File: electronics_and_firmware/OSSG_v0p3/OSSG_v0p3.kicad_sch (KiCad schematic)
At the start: 77 parts, among them IC1 DW01A, J1 USB_B_Micro, J2 External PDM Mic Input, Q1 FS8205A, Q2 Q_NPN_BEC, Q3 Q_NPN_BEC, SW1 SW_SPST, U1 ESP32-PICO-D4, U2 TP4056, U3 XC6222B331MRG, U4 FT232RQ, U5 APX803L-29SA-7, U6 MP23DB01HPTR

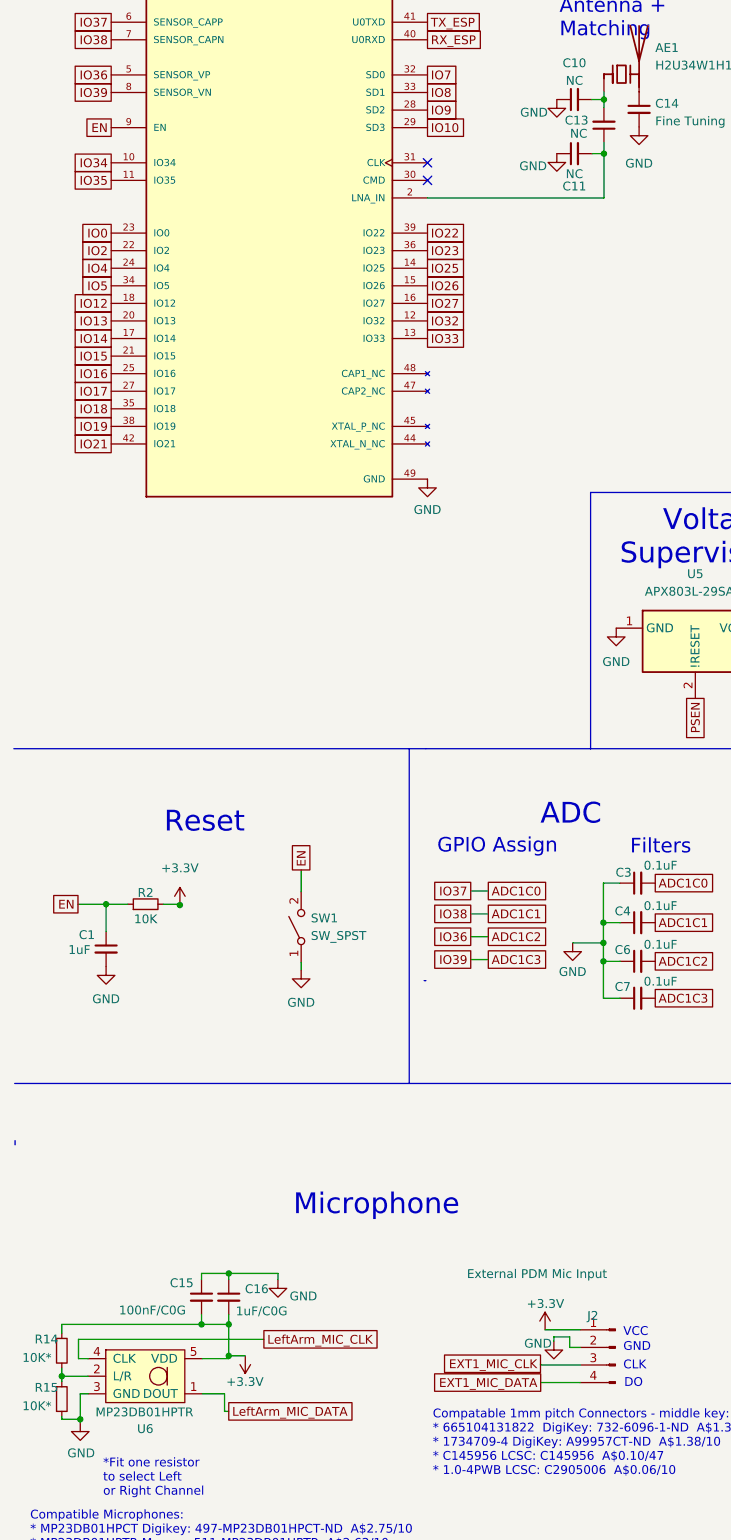
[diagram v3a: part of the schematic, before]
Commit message: start adding in MPN, links, pricing, BOM... digikey and LCSC
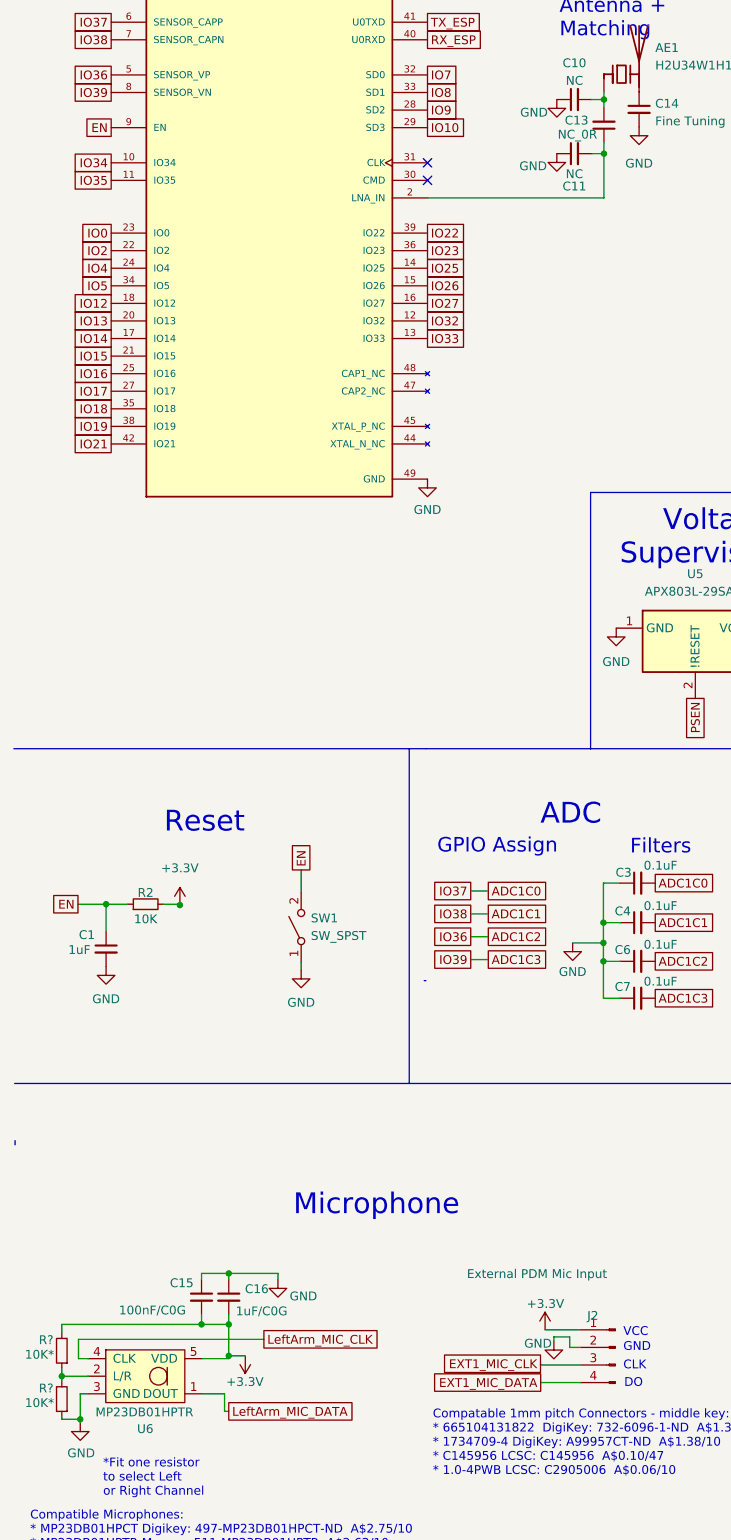
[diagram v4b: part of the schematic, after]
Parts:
- removed R14, R15: 10K*, Resistor_SMD:R_0402_1005Metric, symbol Device:R_Small
- added R? (x2): 10K*, Resistor_SMD:R_0402_1005Metric, symbol Device:R_Small
- AE1: DigiKeyLink (none) -> https://www.digikey.ca/en/products/detail/unictron-technolo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; MPN (none) -> 2047-H2U34W1H1Z0400CT-ND; Price (none) -> 0.9
- C1: DigiKeyLink (none) -> https://www.digikey.ca/en/products/detail/murata-electronic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; MPN (none) -> 490-GRT155C80J105KE01JCT-ND; Price (none) -> 0.0448
- C13: value NC -> NC_0R
- C2: DigiKeyLink (none) -> https://www.digikey.ca/en/products/detail/samsung-electro-m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; MPN (none) -> 1276-1450-1-ND; Price (none) -> 0.1092
- C5: DigiKeyLink (none) -> https://www.digikey.ca/en/products/detail/samsung-electro-m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; MPN (none) -> 1276-1043-1-ND; Price (none) -> 0.006
- IC1: LCSC C351410 -> (none); LCSCLink (none) -> https://lcsc.com/product-detail/Battery-Management-ICs_PUOL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; MPN_LCSC (none) -> C351410; Price (none) -> 0.061
- J1: DigiKeyLink (none) -> https://www.digikey.ca/en/products/detail/molex/1050170001/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; MPN (none) -> WM1399CT-ND; Price (none) -> 1.33
- Q1: LCSCLink (none) -> https://lcsc.com/product-detail/MOSFETs_Fortune-Semicon-FS8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; MPN_LCSC (none) -> C16052; Price (none) -> 0.2665
- R2: DigiKeyLink (none) -> https://www.digikey.ca/en/products/detail/stackpole-electro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; MPN (none) -> RMCF0402JT10K0CT-ND; Price (none) -> 0.018
- R3: DigiKeyLink (none) -> https://www.digikey.ca/en/products/detail/yageo/RC0402JR-07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; MPN (none) -> YAG1279CT-ND; Price (none) -> 0.0182
- SW1: DigiKeyLink (none) -> https://www.digikey.ca/en/products/detail/omron-electronics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; MPN (none) -> SW1103CT-ND; Price (none) -> 1.49
- U1: DigiKeyLink (none) -> https://www.digikey.ca/en/products/detail/espressif-systems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; LCSCLink (none) -> https://lcsc.com/product-detail/RF-Transceiver-ICs_Espressi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; MPN (none) -> 1904-1029-1-ND; MPN_LCSC (none) -> C193707; Price (none) -> 4.1837
- U2: LCSCLink (none) -> https://lcsc.com/product-detail/Battery-Management-ICs_TOPP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; MPN_LCSC (none) -> C21417; Price (none) -> 0.3102
- U3: Price (none) -> 1.25
- U4: LCSCLink (none) -> https://lcsc.com/product-detail/USB-ICs_FTDI-FT232RQ-REEL_C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; MPN_LCSC (none) -> C14090; Price (none) -> 16.1196
- U5: DigiKeyLink (none) -> https://www.digikey.ca/en/products/detail/diodes-incorporat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; MPN (none) -> APX803L-29SA-7DICT-ND; Price (none) -> 0.59
- U6: DigiKeyLink (none) -> https://www.digikey.ca/en/products/detail/stmicroelectronic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; MPN (none) -> 497-MP23DB01HPCT-ND; Price (none) -> 3.31
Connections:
- net +3V3: now also R?.2
- net GND: now also R?.1
- net at U6.2 (L/R): now also R?.1, R?.2

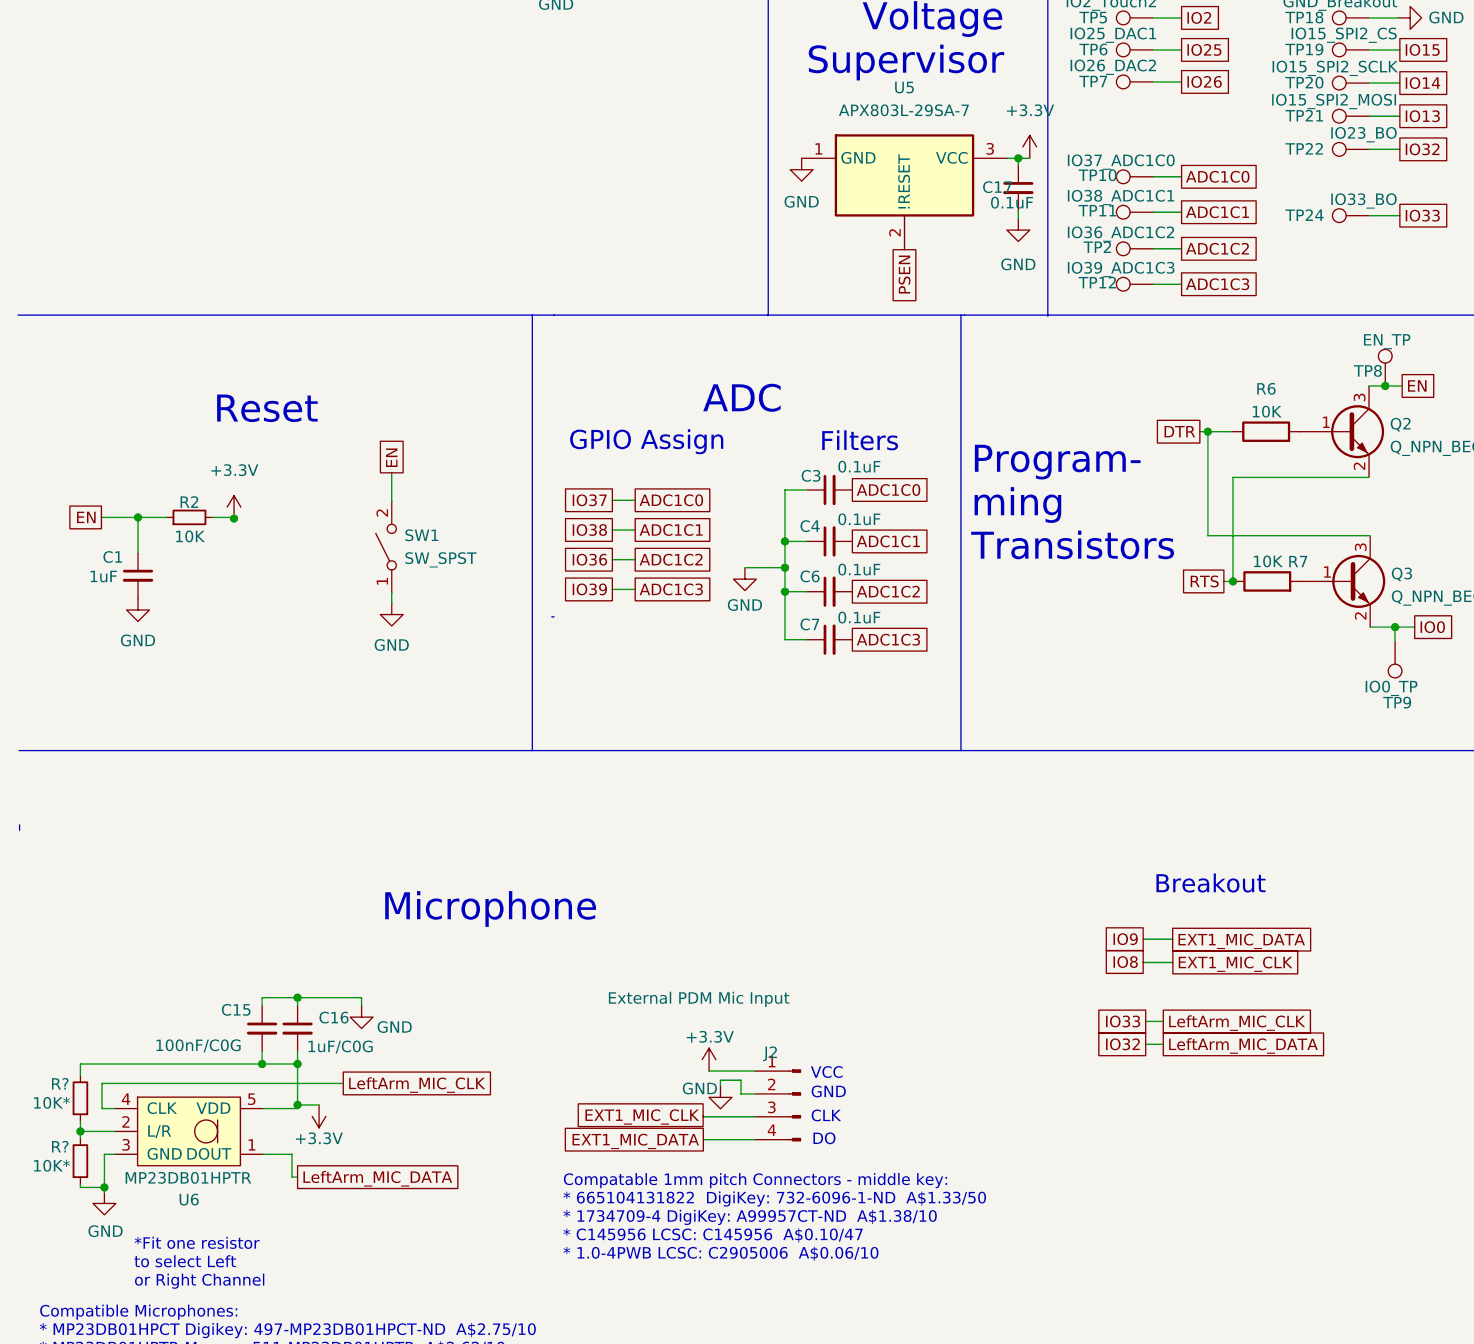
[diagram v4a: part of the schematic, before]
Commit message: add in part numbers and prices for almost all components for LCSC
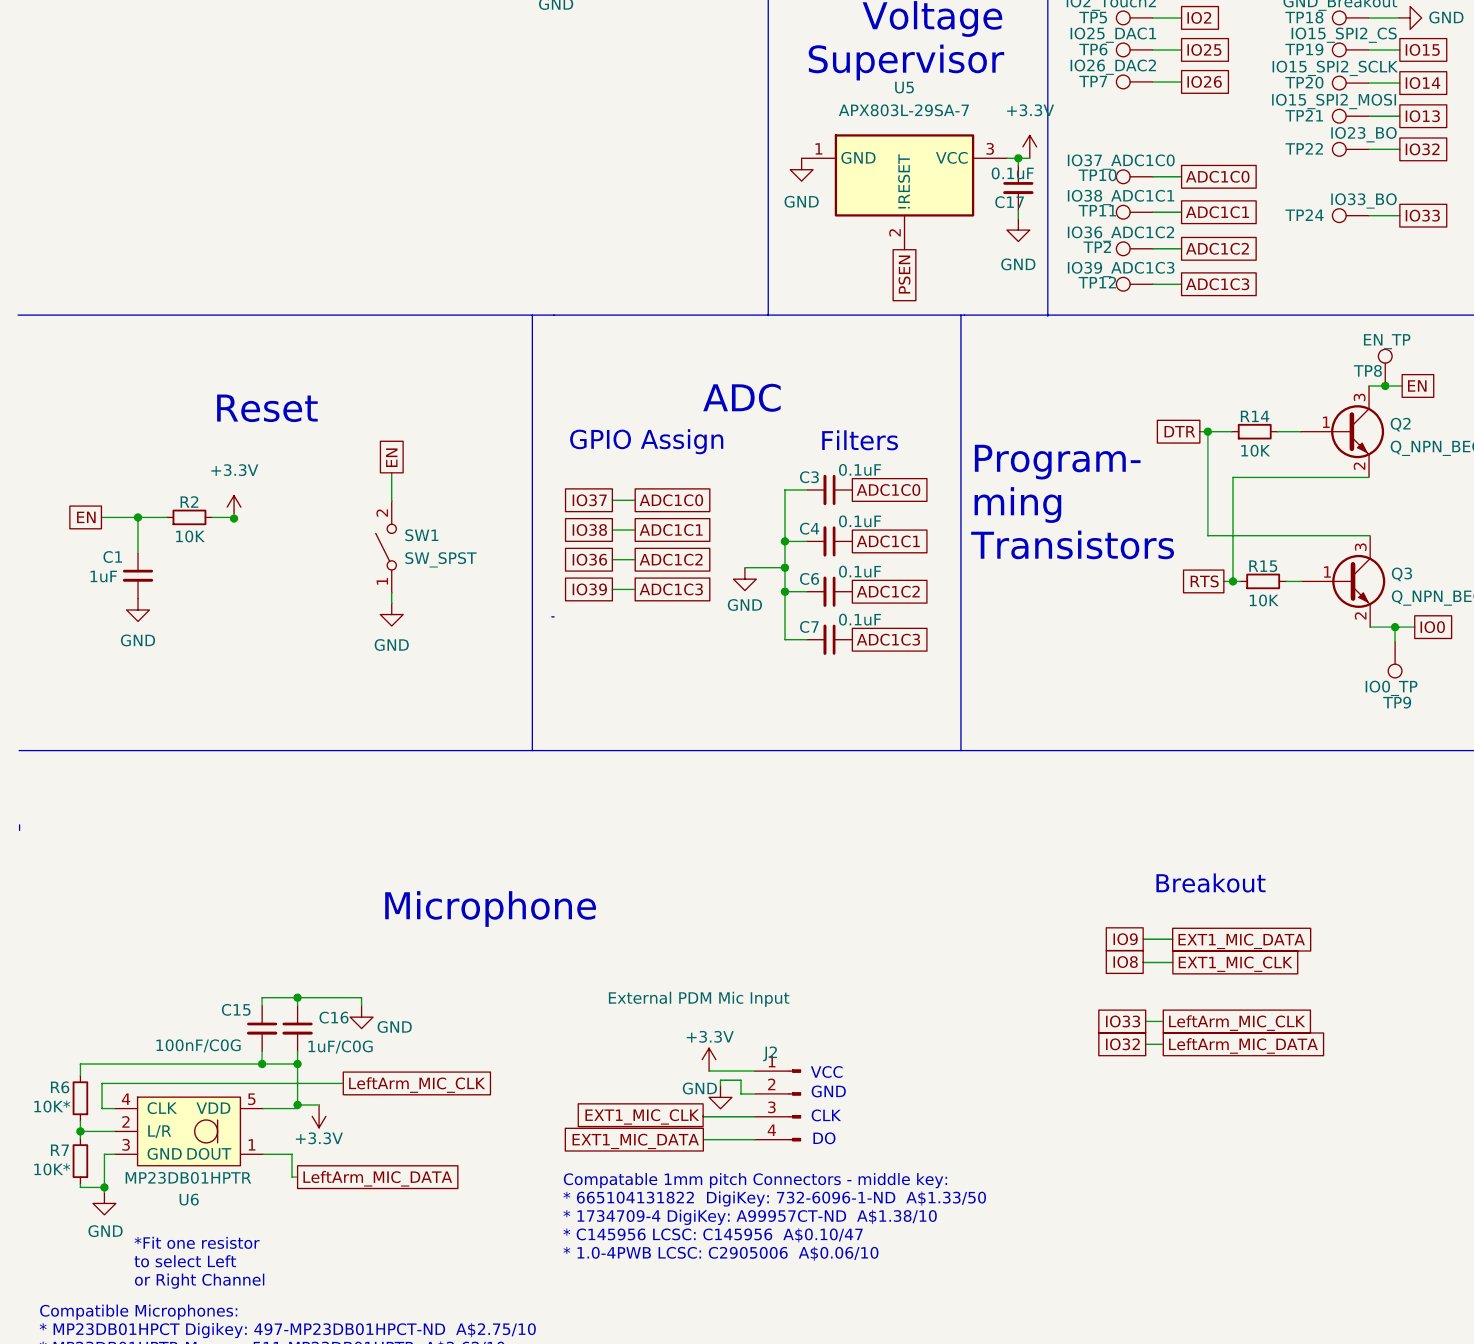
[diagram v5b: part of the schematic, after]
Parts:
- removed R6, R7: 10K, Resistor_SMD:R_0402_1005Metric, symbol Device:R
- removed R? (x2): 10K*, Resistor_SMD:R_0402_1005Metric, symbol Device:R_Small
- added R14, R15: 10K, Resistor_SMD:R_0402_1005Metric, symbol Device:R_Small
- added R6, R7: 10K*, Resistor_SMD:R_0402_1005Metric, symbol Device:R_Small
- AE1: MPN_LCSC (none) -> None
- C1: LCSCLink (none) -> https://lcsc.com/product-detail/Multilayer-Ceramic-Capacito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; MPN_LCSC (none) -> C14445; Price_LCSC (none) -> 0.0018
- C12, C18, C19: MPN_LCSC (none) -> C41851; Price_LCSC (none) -> 0.0008
- C15, C17, C3, C4, C5, C6, C7: LinkLCSC (none) -> https://lcsc.com/product-detail/Multilayer-Ceramic-Capacito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; MPN_LCSC (none) -> C41851; Price_LCSC (none) -> 0.0008
- C16: MPN_LCSC (none) -> C14445; Price_LCSC (none) -> 0.0018
- C2: LCSCLink (none) -> https://lcsc.com/product-detail/Multilayer-Ceramic-Capacito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; MPN_LCSC (none) -> C15525; Price_LCSC (none) -> 0.0057
- C20: LCSCLink (none) -> https://lcsc.com/product-detail/Chip-Resistor-Surface-Mount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; MPN_LCSC (none) -> C258109; Price_LCSC (none) -> 0.0005
- D1: MPN_LCSC (none) -> C2984137; Price_LCSC (none) -> 0.0727
- D2: MPN_LCSC (none) -> C2992661; Price_LCSC (none) -> 0.0738
- D3: MPN_LCSC (none) -> C2987022; Price_LCSC (none) -> 0.0473
- D4: MPN_LCSC (none) -> C2992682; Price_LCSC (none) -> 0.0607
- D5: footprint Diode_SMD:D_0402_1005Metric -> Diode_SMD:D_SOD-123; MPN_LCSC (none) -> C2937163; Price_LCSC (none) -> 0.37
- IC1: Price 0.061 -> (none); Price_LCSC (none) -> 0.061
- J1: LinkLCSC (none) -> https://lcsc.com/product-detail/USB-Connectors_MOLEX-105017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; MPN_LCSC (none) -> C136000; Price_LCSC (none) -> 0.244
- Q2, Q3: LCSCLink (none) -> https://lcsc.com/product-detail/Bipolar-Transistors-BJT_CBI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; MPN_LCSC (none) -> C2836080; Price_LCSC (none) -> 0.0163
- R1: LCSCLink (none) -> https://lcsc.com/product-detail/Chip-Resistor-Surface-Mount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; MPN_LCSC (none) -> C258109; Price_LCSC (none) -> 0.005
- R10, R11: LCSCLink (none) -> https://lcsc.com/product-detail/Chip-Resistor-Surface-Mount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; MPN_LCSC (none) -> C453619; Price_LCSC (none) -> 0.0005
- R12: LinkLCSC (none) -> https://lcsc.com/product-detail/Chip-span-style-background-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; MPN_LCSC (none) -> C273339; Price_LCSC (none) -> 0.0006
- R13: LCSCLink (none) -> https://lcsc.com/product-detail/Chip-span-style-background-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; MPN_LCSC (none) -> C423115; Price_LCSC (none) -> 0.0005
- R2: LCSCLink (none) -> https://lcsc.com/product-detail/Chip-span-style-background-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; MPN_LCSC (none) -> C2906885; Price_LCSC (none) -> 0.0005
- R3: LCSCLink (none) -> https://lcsc.com/product-detail/Chip-span-style-background-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; MPN_LCSC (none) -> C2906877; Price_LCSC (none) -> 0.0005
- R4: LinkLCSC (none) -> https://lcsc.com/product-detail/Chip-Resistor-Surface-Mount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; MPN_LCSC (none) -> C2906899; Price_LCSC (none) -> 0.0005
- R5: LCSCLink (none) -> https://lcsc.com/product-detail/Chip-Resistor-Surface-Mount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; MPN_LCSC (none) -> C43251; Price_LCSC (none) -> 0.0006
- R8: LCSCLink (none) -> https://lcsc.com/product-detail/Chip-Resistor-Surface-Mount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; MPN_LCSC (none) -> C105876; Price_LCSC (none) -> 0.0005
- R9: LCSCLink (none) -> https://lcsc.com/product-detail/Chip-Resistor-Surface-Mount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; MPN_LCSC (none) -> C105876; Price_LCSC (none) -> 0.005
- U2: Price 0.3102 -> (none); Price_LCSC (none) -> 0.3102
- U3: LCSCLink (none) -> https://lcsc.com/product-detail/Linear-Voltage-Regulators-s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; MPN_LCSC (none) -> C427602; Price_LCSC (none) -> 0.58
- U4: Price 16.1196 -> (none); Price_LCSC (none) -> 16.1196
- U5: LCSCLink (none) -> https://lcsc.com/product-detail/Monitors-Reset-Circuits_Chi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; MPN_LCSC (none) -> CL7809SS; Price_LCSC (none) -> 0.0395
- U6: LCSCLink (none) -> https://www.lcsc.com/product-detail/MEMS-Microphones_INGHAi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; MPN_LCSC (none) -> C498192; Price_LCSC (none) -> 1.0964
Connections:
- net +3V3: now also R6.2
- net ADC1C0: now also C3.1; no longer C3.2
- net ADC1C1: now also C4.1; no longer C4.2
- net ADC1C2: now also C6.1; no longer C6.2
- net ADC1C3: now also C7.1; no longer C7.2
- net DTR: now also R14.1
- net GND: now also C3.2, C4.2, C6.2, C7.2, R7.1; no longer C3.1, C4.1, C6.1, C7.1
- net RTS: now also R15.1
- net at Q3.1 (B): now also R15.2
- net at Q2.1 (B): now also R14.2
- net at U6.2 (L/R): now also R6.1, R7.2
